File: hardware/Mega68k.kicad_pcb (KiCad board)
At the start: 2 copper layers, 101.8 x 68.2 mm, 23 parts, among them IC1 MC68008FN8, J3 SD Card, J4 Bus, J5 Serial 1, SW1 ARD RESET, SW2 CPU_RESET, U1 AS6C4008-55PCN, U2 MC68681FN, X1 CXO_DIP8, Y1 3.6864

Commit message: Some cleanup
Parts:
- J4: value Bus -> Debug
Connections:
- C6 pad 2: unconnected-(C6-Pad2) -> GND
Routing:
- net GND: track 348.0 -> 349.9 mm
- net /D0: track 245.7 -> 246.5 mm

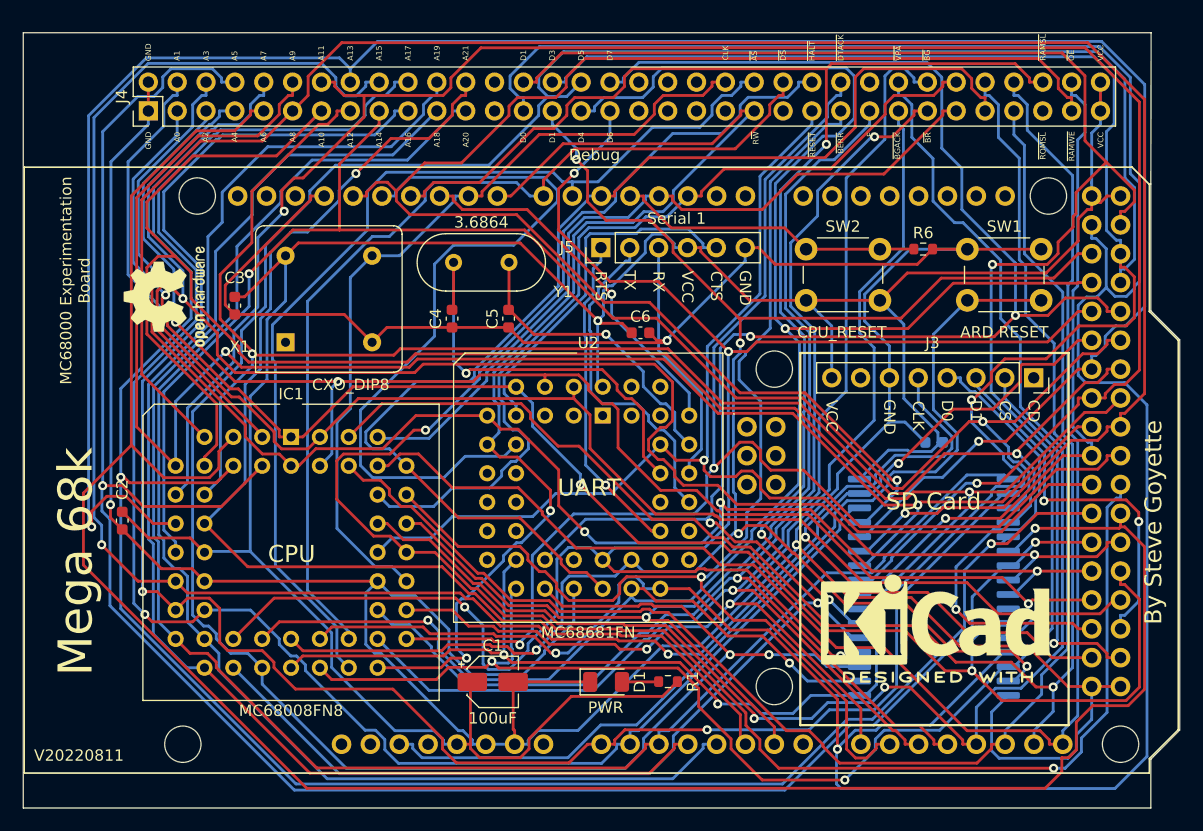
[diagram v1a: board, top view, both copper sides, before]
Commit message: Updated Mega68k freerun sketch to work with rev V20220811
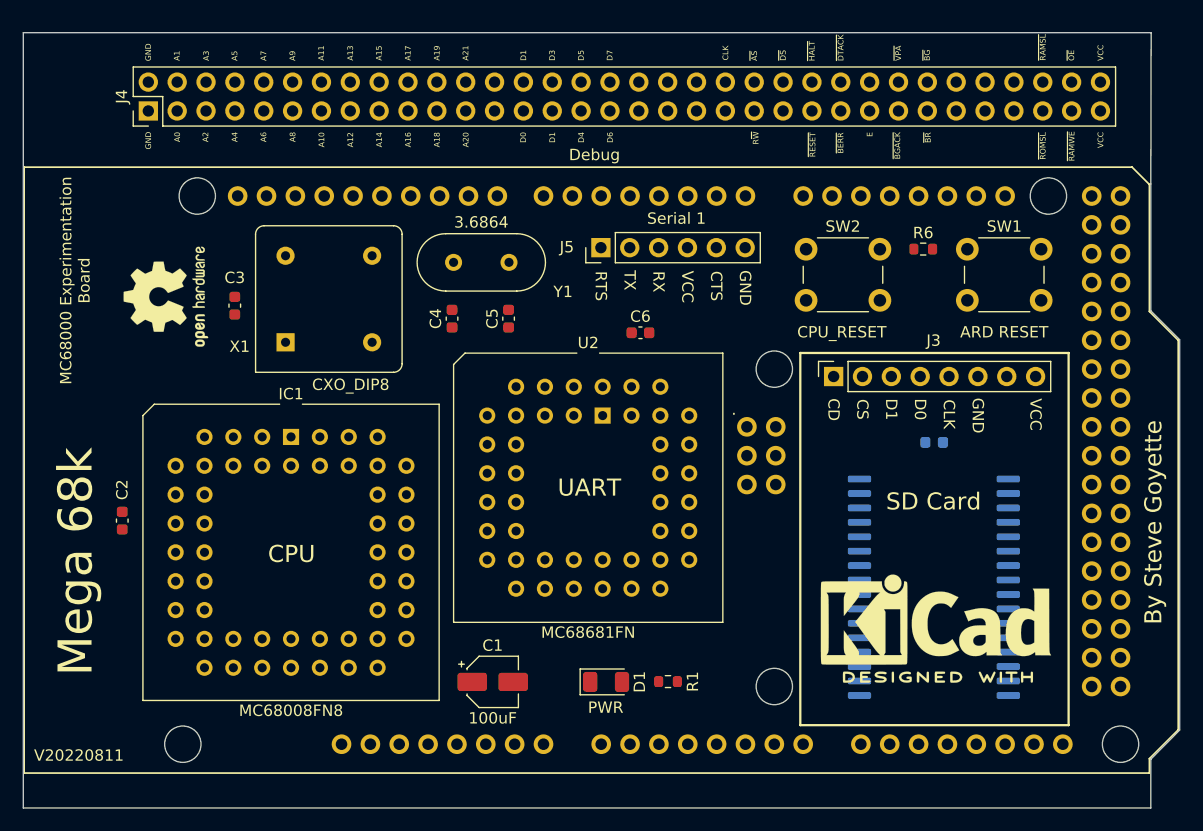
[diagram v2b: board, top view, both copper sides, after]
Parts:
- moved J3 17.6 mm to (119.5, 76.6), turned to 90 degrees
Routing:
- net GND: track 349.9 -> 0.00 mm, vias 3 -> 0
- net /D0: track 246.5 -> 0.00 mm, vias 2 -> 0
- net VCC: track 243.9 -> 0.00 mm, vias 1 -> 0
- net /D5: track 234.0 -> 0.00 mm, vias 2 -> 0
- net /D7: track 203.8 -> 0.00 mm, vias 4 -> 0
- net /D1: track 203.3 -> 0.00 mm, vias 3 -> 0
- net /A13: track 200.1 -> 0.00 mm, vias 2 -> 0
- net /A6: track 196.4 -> 0.00 mm, vias 1 -> 0
- net /D3: track 190.5 -> 0.00 mm, vias 3 -> 0
- net /D4: track 178.8 -> 0.00 mm, vias 3 -> 0
- net /A8: track 177.9 -> 0.00 mm, vias 1 -> 0
- net /A5: track 177.4 -> 0.00 mm, vias 2 -> 0
- net /A11: track 176.2 -> 0.00 mm, vias 2 -> 0
- net /A7: track 172.9 -> 0.00 mm, vias 2 -> 0
- net /A15: track 171.8 -> 0.00 mm, vias 3 -> 0
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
